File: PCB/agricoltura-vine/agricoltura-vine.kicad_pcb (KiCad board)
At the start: 4 copper layers, 110 x 80 mm, 114 parts, among them K1 G5LE-14_DC5, K2 G5LE-14_DC5, Q1 IRLML6346TRPBF, Q2 IRLML6346TRPBF, SW1 TL3301NF260QG, T1 BU2032SM-JJ-GTR, T10 BM04B-SRSS-TB(LF)(SN), T11 BM04B-SRSS-TB(LF)(SN), T12 BM04B-SRSS-TB(LF)(SN), T13 BM04B-SRSS-TB(LF)(SN), T14 BM04B-SRSS-TB(LF)(SN), T15 BM04B-SRSS-TB(LF)(SN), T16 0395121002, T17 0395121004, T18 0395121004, T19 TSW-108-07-G-T, T2 20021121-00010C4LF, T20 0010897080, T22 0395121006, T3 0675031020, T4 BM04B-SRSS-TB(LF)(SN), T5 BM04B-SRSS-TB(LF)(SN), T6 BM04B-SRSS-TB(LF)(SN), T7 BM04B-SRSS-TB(LF)(SN), T8 BM04B-SRSS-TB(LF)(SN), T9 BM04B-SRSS-TB(LF)(SN), U1 STM32F446RET6, U10 ZXGD3009E6TA, U2 74HC4052D, U3 TCA9548APWR, U4 AP63203WU-7, U5 AP63205WU-7, U6 MAX13450EAUD+, U7 MAX13450EAUD+, U8 TCA6416ARTWR, U9 ZXGD3009E6TA, X1 ABM3B-8.000MHZ-B2-T, X2 ABS07-32.768KHZ-9-T

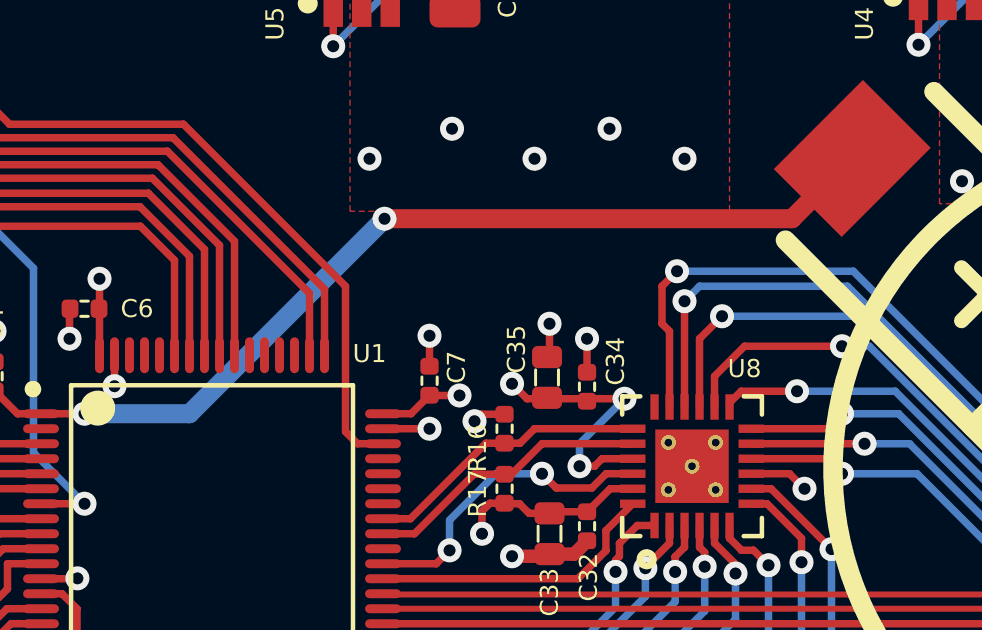
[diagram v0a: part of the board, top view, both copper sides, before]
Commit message: Netlabels and Datasheets
Removed datasheets for parts no longer in design, added datasheet for RS485 transceiver. Added netlabels for RS485 signals.
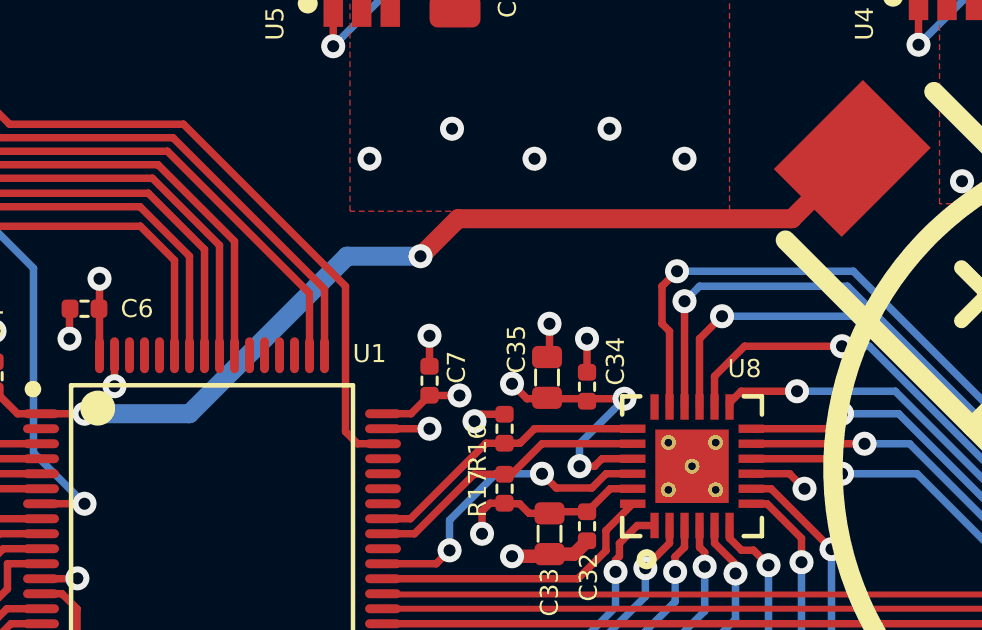
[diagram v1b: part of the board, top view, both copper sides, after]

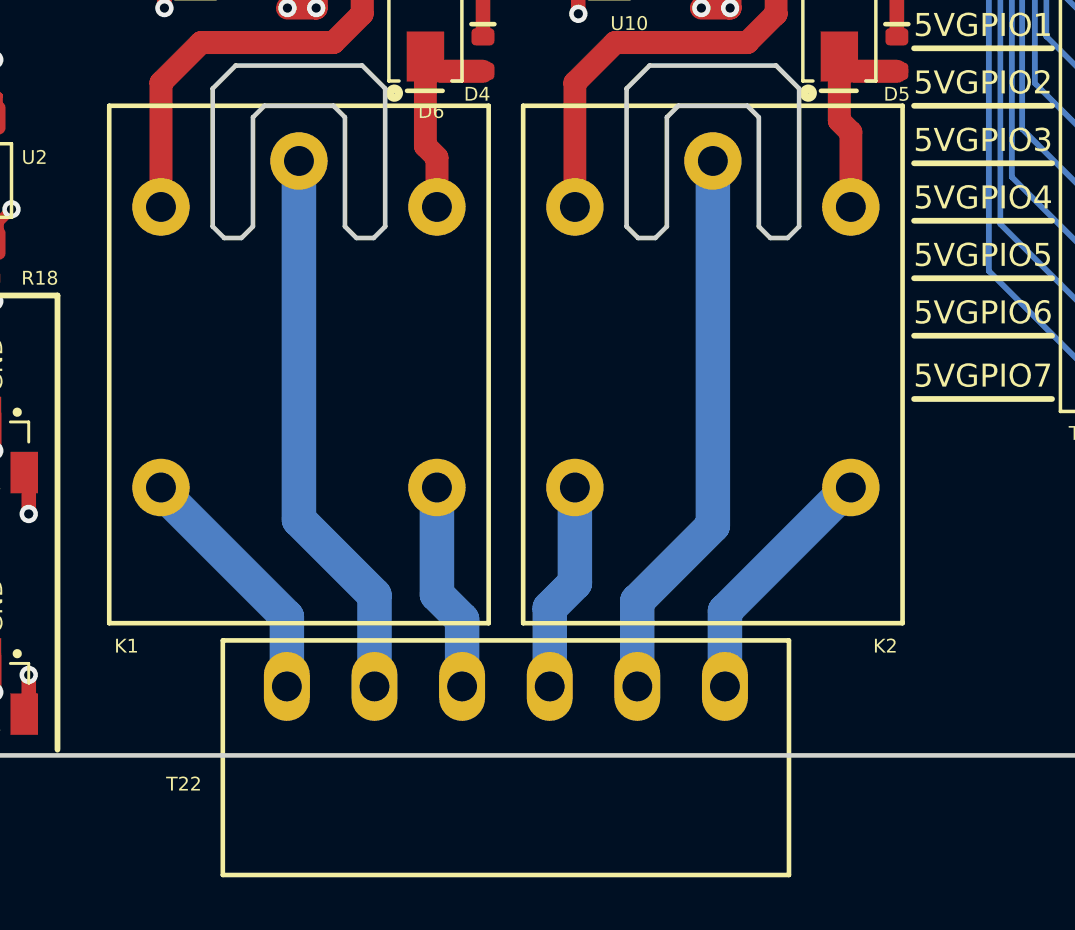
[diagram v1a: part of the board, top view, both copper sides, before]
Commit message: Connector Swap
Switched over to dedicated connectors per relay
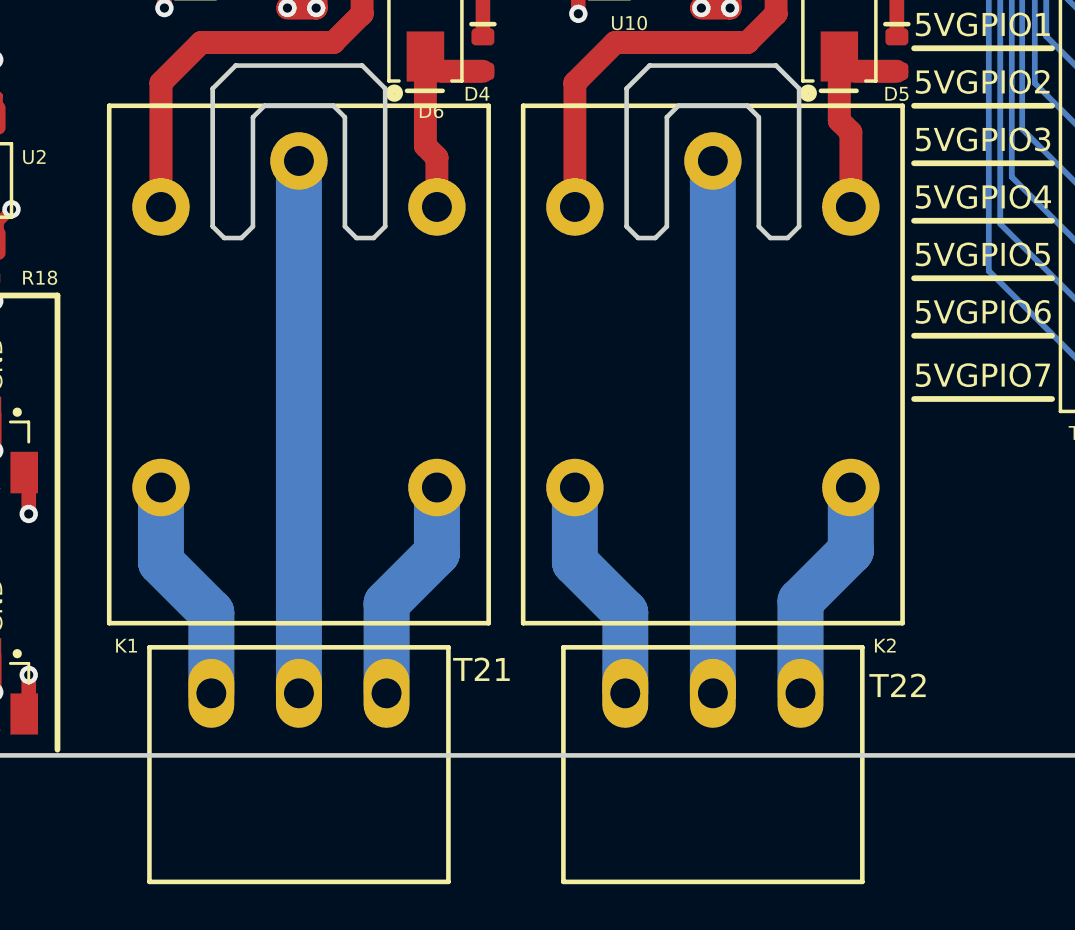
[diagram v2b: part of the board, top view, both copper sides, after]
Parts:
- added T21: 0395121003, AVR-KiCAD-Lib-Connectors:0395121003, F.Cu at (172.5, 137.3)
- T22: value 0395121006 -> 0395121003; footprint AVR-KiCAD-Lib-Connectors:0395121006 -> AVR-KiCAD-Lib-Connectors:0395121003
- moved T22 9.00 mm to (190.5, 137.3)
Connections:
- T22 pad 1: Net-(K1-Pad4) -> Net-(K2-Pad4)
- T22 pad 2: Net-(K1-Pad1) -> Net-(K2-Pad1)
- T22 pad 3: Net-(K1-Pad3) -> Net-(K2-Pad3)
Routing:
- net Net-(K1-Pad4): track 11.1 -> 9.86 mm
- net Net-(K2-Pad3): track 11.0 -> 9.86 mm
- net Net-(K2-Pad1): track 24.2 -> 23.2 mm
- net Net-(K1-Pad1): track 24.3 -> 23.5 mm
- net Net-(K2-Pad4): track 9.10 -> 9.86 mm
- net Net-(K1-Pad3): track 9.21 -> 9.86 mm

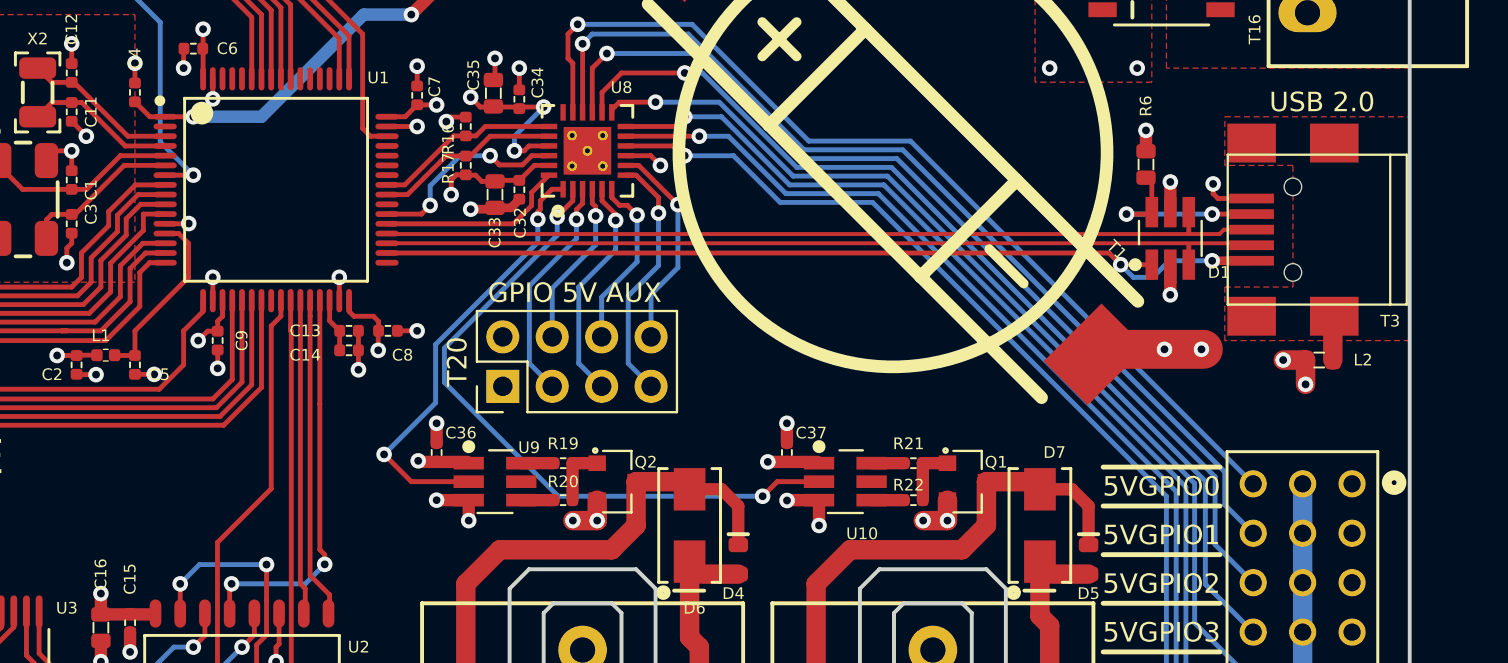
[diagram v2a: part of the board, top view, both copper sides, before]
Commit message: EEPROM
Added EEPROM chip to design, also beefed up USB grounding and shock protection
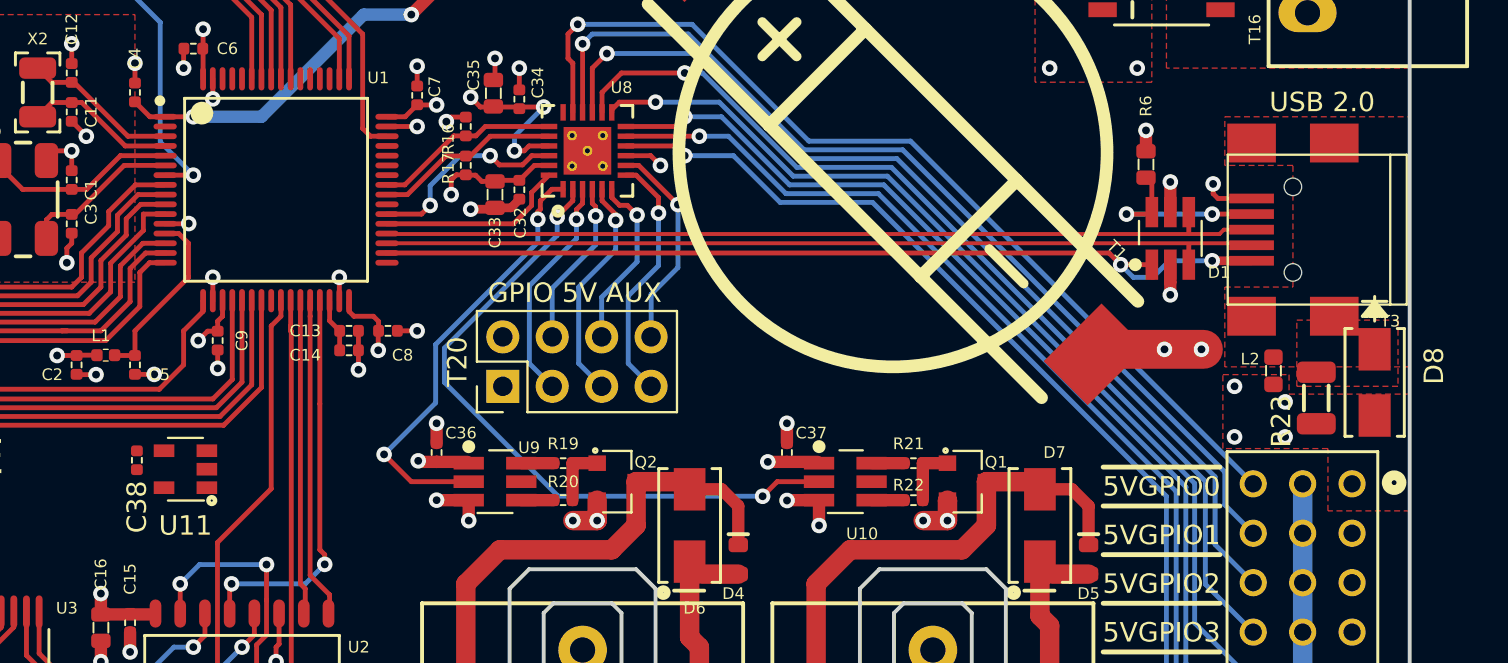
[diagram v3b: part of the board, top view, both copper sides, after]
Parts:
- added C38: C0402C104K9PACTU, AVR-KiCAD-Lib-Resistors:R0402, F.Cu at (149.6, 104.4)
- added D8: SMAJ30CA, AVR-KiCAD-Lib-Diodes:SMAJ30CA, F.Cu at (213.2, 100.4)
- added R23: RC1206FR-071ML, AVR-KiCAD-Lib-Resistors:R1206, F.Cu at (210.2, 101.2)
- added U11: AT24C16D-STUM-T, AVR-KiCAD-Lib-ICs:SOT-23-5, F.Cu at (152.1, 104.9)
- moved L2 2.41 mm to (208.0, 99.8), turned to 270 degrees
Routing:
- net GND: track 152.8 -> 150.4 mm, vias 121 -> 123
- net Net-(D8-Pad1): track 2.28 -> 0.11 mm

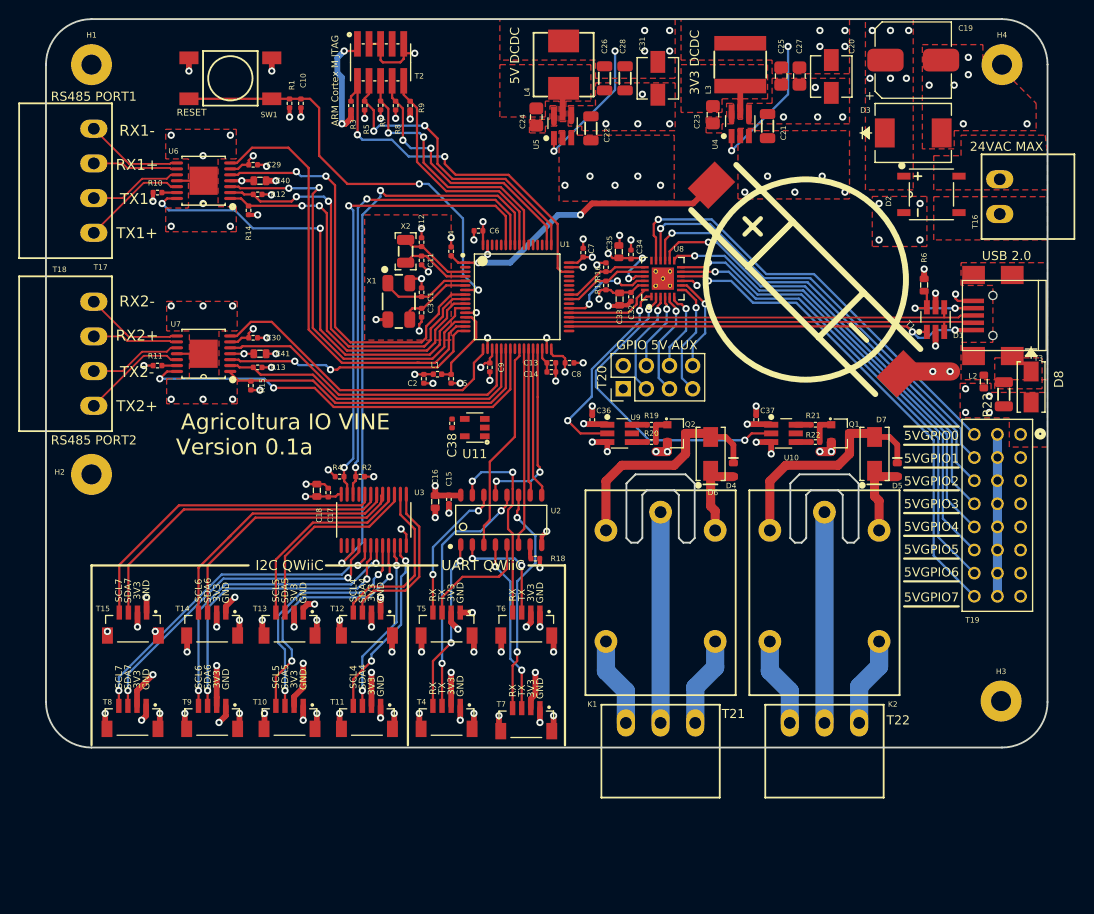
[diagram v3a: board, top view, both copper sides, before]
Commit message: Added EEProm
Eeprom added and routed in circuit board, USB resitors added. TVS diodes and pullups added to I2C ports not yet placed.
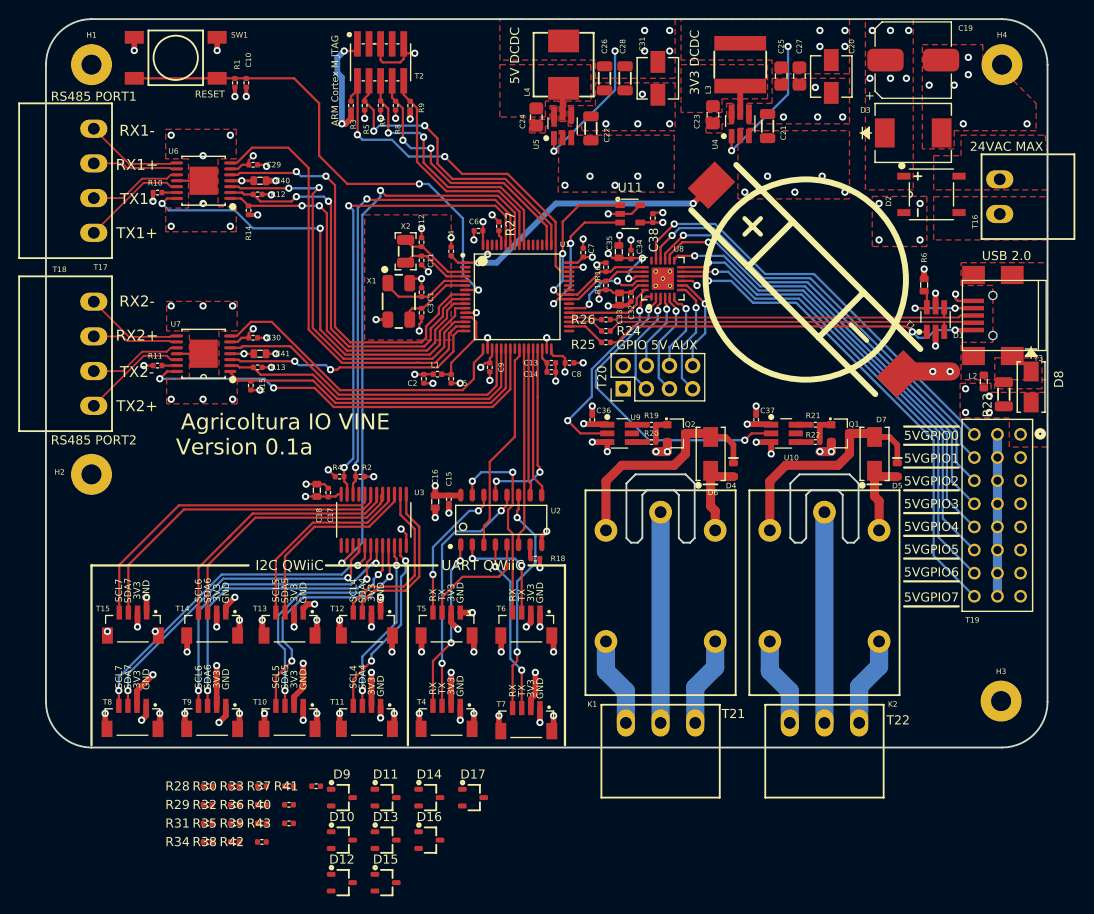
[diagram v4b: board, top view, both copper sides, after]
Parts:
- added D10: PESD3V3L2BT,215, AVR-KiCAD-Lib-Diodes:SOT-23, F.Cu at (137.5, 150.2)
- added D11: PESD3V3L2BT,215, AVR-KiCAD-Lib-Diodes:SOT-23, F.Cu at (142.3, 145.5)
- added D12: PESD3V3L2BT,215, AVR-KiCAD-Lib-Diodes:SOT-23, F.Cu at (137.5, 154.8)
- added D13: PESD3V3L2BT,215, AVR-KiCAD-Lib-Diodes:SOT-23, F.Cu at (142.3, 150.2)
- added D14: PESD3V3L2BT,215, AVR-KiCAD-Lib-Diodes:SOT-23, F.Cu at (147.1, 145.5)
- added D15: PESD3V3L2BT,215, AVR-KiCAD-Lib-Diodes:SOT-23, F.Cu at (142.3, 154.8)
- added D16: PESD3V3L2BT,215, AVR-KiCAD-Lib-Diodes:SOT-23, F.Cu at (147.1, 150.2)
- added D17: PESD3V3L2BT,215, AVR-KiCAD-Lib-Diodes:SOT-23, F.Cu at (151.9, 145.5)
- added D9: PESD3V3L2BT,215, AVR-KiCAD-Lib-Diodes:SOT-23, F.Cu at (137.5, 145.5)
- added R24: RC0402FR-0722RL, AVR-KiCAD-Lib-Resistors:R0402, F.Cu at (166.5, 94.2)
- added R25: RC0402FR-0710KL, AVR-KiCAD-Lib-Resistors:R0402, F.Cu at (166.5, 95.5)
- added R26: RC0402FR-0722RL, AVR-KiCAD-Lib-Resistors:R0402, F.Cu at (166.5, 93.0)
- added R27: RC0402FR-0710KL, AVR-KiCAD-Lib-Resistors:R0402, F.Cu at (154.8, 82.8)
- added R28: RC0402FR-074K7L, AVR-KiCAD-Lib-Resistors:R0402, F.Cu at (122.8, 144.2)
- added R29: RC0402FR-074K7L, AVR-KiCAD-Lib-Resistors:R0402, F.Cu at (122.8, 146.3)
- added R30: RC0402FR-074K7L, AVR-KiCAD-Lib-Resistors:R0402, F.Cu at (125.7, 144.2)
- added R31: RC0402FR-074K7L, AVR-KiCAD-Lib-Resistors:R0402, F.Cu at (122.8, 148.3)
- added R32: RC0402FR-074K7L, AVR-KiCAD-Lib-Resistors:R0402, F.Cu at (125.7, 146.3)
- added R33: RC0402FR-074K7L, AVR-KiCAD-Lib-Resistors:R0402, F.Cu at (128.7, 144.2)
- added R34: RC0402FR-074K7L, AVR-KiCAD-Lib-Resistors:R0402, F.Cu at (122.8, 150.4)
- added R35: RC0402FR-074K7L, AVR-KiCAD-Lib-Resistors:R0402, F.Cu at (125.7, 148.3)
- added R36: RC0402FR-074K7L, AVR-KiCAD-Lib-Resistors:R0402, F.Cu at (128.7, 146.3)
- added R37: RC0402FR-074K7L, AVR-KiCAD-Lib-Resistors:R0402, F.Cu at (131.7, 144.2)
- added R38: RC0402FR-074K7L, AVR-KiCAD-Lib-Resistors:R0402, F.Cu at (125.7, 150.4)
- added R39: RC0402FR-074K7L, AVR-KiCAD-Lib-Resistors:R0402, F.Cu at (128.7, 148.3)
- added R40: RC0402FR-074K7L, AVR-KiCAD-Lib-Resistors:R0402, F.Cu at (131.7, 146.3)
- added R41: RC0402FR-074K7L, AVR-KiCAD-Lib-Resistors:R0402, F.Cu at (134.7, 144.2)
- added R42: RC0402FR-074K7L, AVR-KiCAD-Lib-Resistors:R0402, F.Cu at (128.7, 150.4)
- added R43: RC0402FR-074K7L, AVR-KiCAD-Lib-Resistors:R0402, F.Cu at (131.7, 148.3)
- moved C38 31.5 mm to (171.7, 81.8), turned to 90 degrees
- moved U11 29.0 mm to (169.2, 81.4), turned to 0 degrees
- moved C10 6.41 mm to (127.0, 67.0)
- moved R1 6.41 mm to (125.8, 67.0)
- moved SW1 6.41 mm to (119.2, 64.2)
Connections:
- C11 pad 2: Net-(C11-Pad2) -> /STM32F446RET Controller/OSC32_OUT
- U1 pad 34: /STM32F446RET Controller/VBUS -> /STM32F446RET Controller/MCU_VBUS
- U1 pad 35: /STM32F446RET Controller/D- -> /STM32F446RET Controller/MCU_D-
- U1 pad 36: /STM32F446RET Controller/D+ -> /STM32F446RET Controller/MCU_D+
- U11 pad 1: Net-(U11-Pad1) -> /5V IO Interfaces/IO_SCL
- U11 pad 3: Net-(U11-Pad3) -> /5V IO Interfaces/IO_SDA
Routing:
- net /5V IO Interfaces/IO_SCL: track 9.57 -> 26.4 mm, vias 0 -> 2
- net /5V IO Interfaces/IO_SDA: track 9.57 -> 25.7 mm, vias 0 -> 2
- net +3V3: track 111.7 -> 124.1 mm, vias 43 -> 44
- net /STM32F446RET Controller/NRST: track 48.6 -> 55.9 mm
- net GND: track 150.4 -> 156.6 mm, vias 123 -> 126
- net /STM32F446RET Controller/D+: track 45.6 -> 41.2 mm
- net /STM32F446RET Controller/MCU_VBUS: track 0.00 -> 4.29 mm
- net /STM32F446RET Controller/D-: track 45.5 -> 41.4 mm
- net /STM32F446RET Controller/MCU_D-: track 0.00 -> 4.00 mm
- net /STM32F446RET Controller/VBUS: track 46.9 -> 43.1 mm
- net /STM32F446RET Controller/MCU_D+: track 0.00 -> 3.71 mm
- net Net-(T19-Pad3): track 49.3 -> 47.4 mm
- net Net-(R27-Pad1): track 0.00 -> 1.67 mm
- net Net-(T19-Pad6): track 49.8 -> 48.2 mm
- net Net-(T19-Pad9): track 49.8 -> 48.8 mm
